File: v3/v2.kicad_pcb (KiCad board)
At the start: 2 copper layers, 82 parts, among them J1 Conn_01x05_Pin, SW1 SW_Push, SW10 SW_Push, SW11 SW_Push, SW12 SW_Push, SW13 SW_Push, SW14 SW_Push, SW15 SW_Push, SW16 SW_Push, SW17 SW_Push, SW18 SW_Push, SW19 SW_Push, SW2 SW_Push, SW20 SW_Push, SW21 SW_Push, SW22 SW_Push, SW23 SW_Push, SW24 SW_Push, SW25 SW_Push, SW26 SW_Push, SW27 SW_Push, SW28 SW_Push, SW29 SW_Push, SW3 SW_Push, SW30 SW_Push, SW31 SW_Push, SW32 SW_Push, SW33 RotaryEncoder_Switch, SW4 SW_Push, SW5 SW_Push, SW6 SW_Push, SW7 SW_Push, SW8 SW_Push, SW9 SW_Push, U1 nice_nano_left

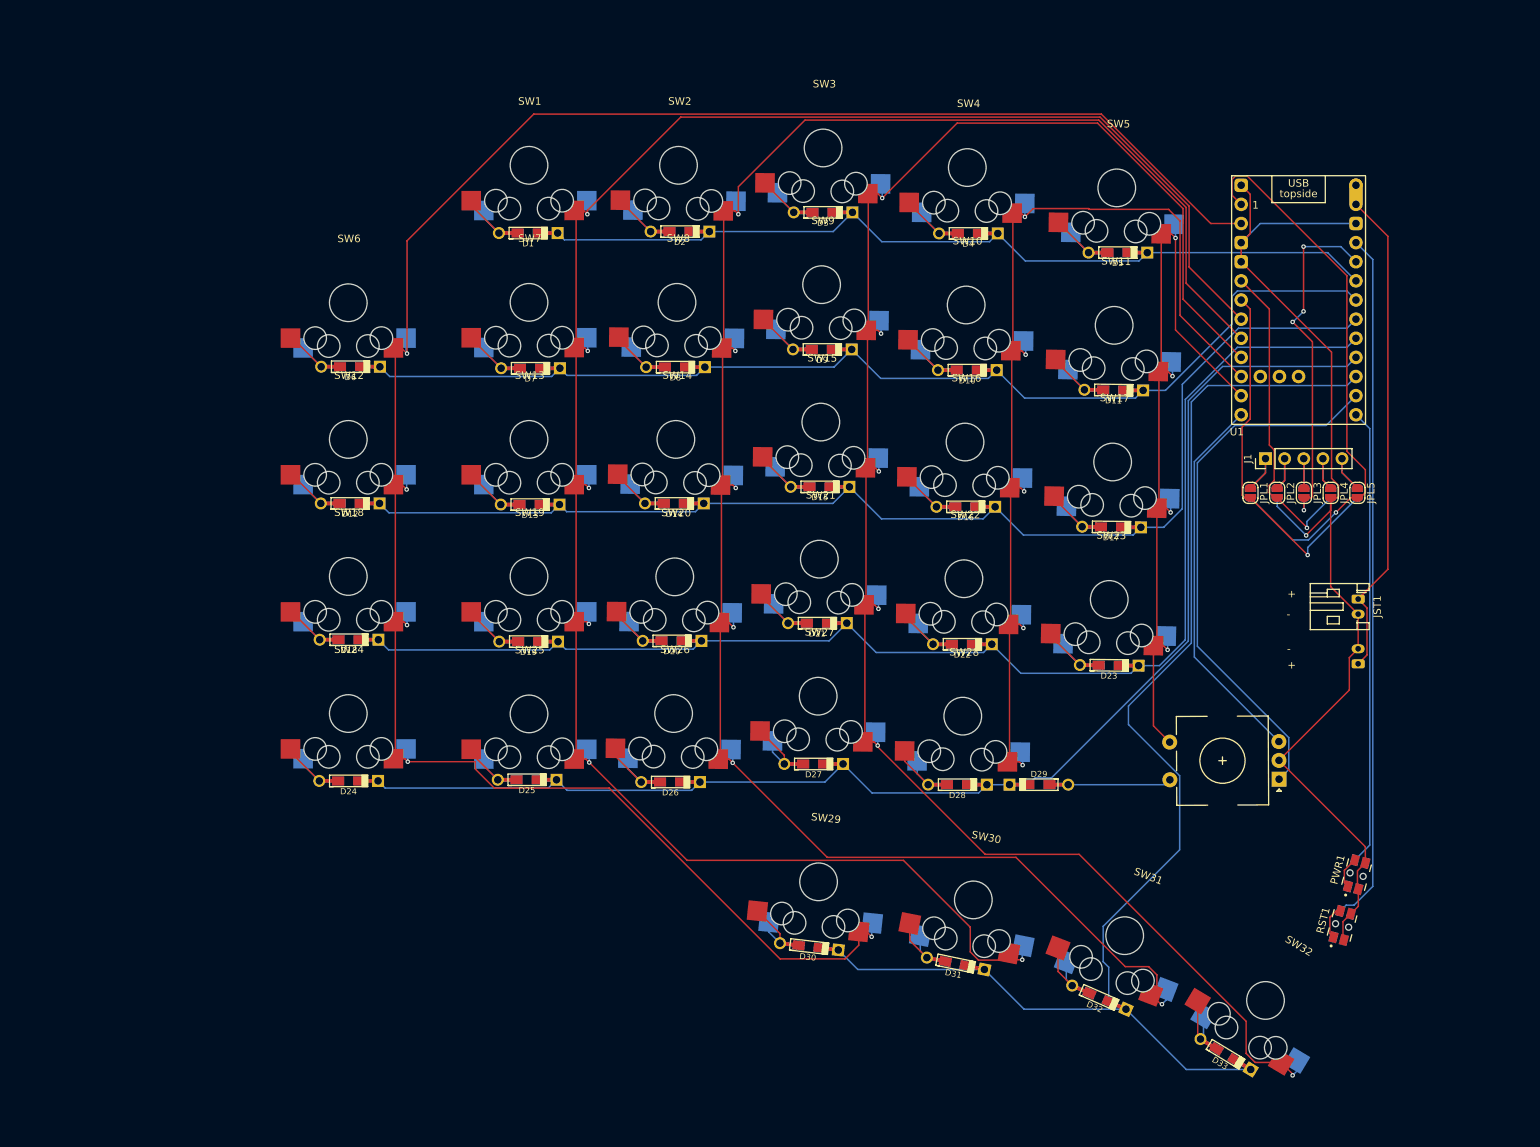
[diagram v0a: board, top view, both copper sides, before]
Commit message: added edge cuts and started cad again
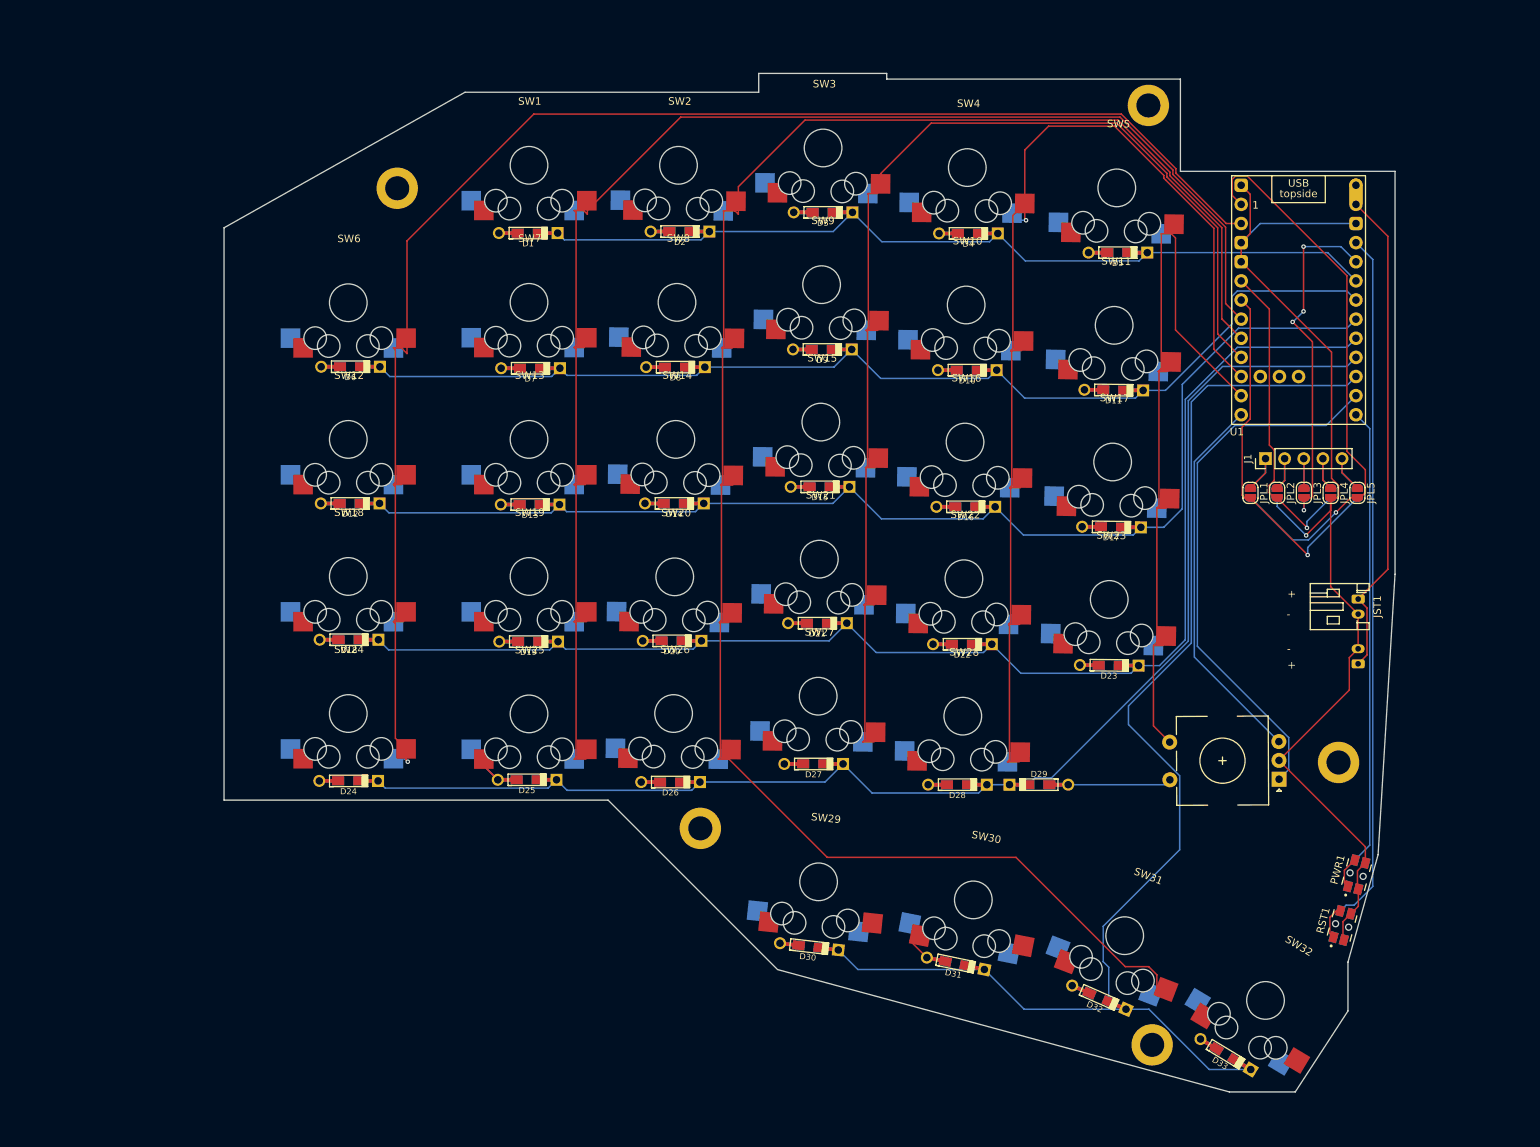
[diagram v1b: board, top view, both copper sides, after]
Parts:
- added REF**: MountingHole_3.2mm_M3_ISO14580_Pad, Keebio-Parts.pretty-master:MountingHole_3.2mm_M3_ISO14580_Pad, F.Cu at (250.8, 167.5)
- added REF**: MountingHole_3.2mm_M3_ISO14580_Pad, Keebio-Parts.pretty-master:MountingHole_3.2mm_M3_ISO14580_Pad, F.Cu at (250.2, 42.8)
- added REF**: MountingHole_3.2mm_M3_ISO14580_Pad, Keebio-Parts.pretty-master:MountingHole_3.2mm_M3_ISO14580_Pad, F.Cu at (275.5, 130.0)
- added REF**: MountingHole_3.2mm_M3_ISO14580_Pad, Keebio-Parts.pretty-master:MountingHole_3.2mm_M3_ISO14580_Pad, F.Cu at (150.5, 53.8)
- added REF**: MountingHole_3.2mm_M3_ISO14580_Pad, Keebio-Parts.pretty-master:MountingHole_3.2mm_M3_ISO14580_Pad, F.Cu at (190.8, 138.8)
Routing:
- net Col 4: track 243.3 -> 153.8 mm, vias 6 -> 0
- net Col 1: track 287.5 -> 201.9 mm, vias 5 -> 1
- net Col 2: track 274.4 -> 191.6 mm, vias 6 -> 0
- net Col 3: track 260.3 -> 245.2 mm, vias 6 -> 0
- net Col 6: track 109.6 -> 99.4 mm, vias 4 -> 0
- net Net-(D26-A): track 9.79 -> 0.00 mm
- net Net-(D24-A): track 9.67 -> 0.00 mm
- net Net-(D2-A): track 9.66 -> 0.00 mm
- net Net-(D1-A): track 9.65 -> 0.00 mm
- net Net-(D28-A): track 9.54 -> 0.00 mm
- net Net-(D23-A): track 9.53 -> 0.00 mm
- net Net-(D4-A): track 9.52 -> 0.00 mm
- net Net-(D27-A): track 9.43 -> 0.00 mm
- net Net-(D7-A): track 9.40 -> 0.00 mm
- net Net-(D10-A): track 9.35 -> 0.00 mm
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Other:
- board outline added: 155.5 x 135.2 mm

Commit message: fix lots of reversible error stuff
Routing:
- net Col 4: track 153.8 -> 255.2 mm, vias 0 -> 6
- net Col 2: track 191.6 -> 281.7 mm, vias 0 -> 6
- net Col 1: track 201.9 -> 284.0 mm, vias 1 -> 5
- net Col 3: track 245.2 -> 265.2 mm, vias 0 -> 6
- net Col 5: track 147.0 -> 165.1 mm, vias 1 -> 5
- net Col 6: track 99.4 -> 112.9 mm, vias 0 -> 4
- net Net-(D22-A): track 0.00 -> 9.01 mm, vias 0 -> 1
- net Net-(D23-A): track 0.00 -> 8.94 mm, vias 0 -> 1
- net Net-(D4-A): track 0.00 -> 8.91 mm, vias 0 -> 1
- net Net-(D9-A): track 0.00 -> 8.90 mm, vias 0 -> 1
- net Net-(D11-A): track 0.00 -> 8.84 mm, vias 0 -> 1
- net Net-(D26-A): track 0.00 -> 8.70 mm, vias 0 -> 1
- net Net-(D5-A): track 0.00 -> 8.69 mm, vias 0 -> 1
- net Net-(D17-A): track 0.00 -> 8.69 mm, vias 0 -> 1
- net Net-(D15-A): track 0.00 -> 8.67 mm, vias 0 -> 1
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
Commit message: added branding
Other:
- board text added: "Foxxboard V3"

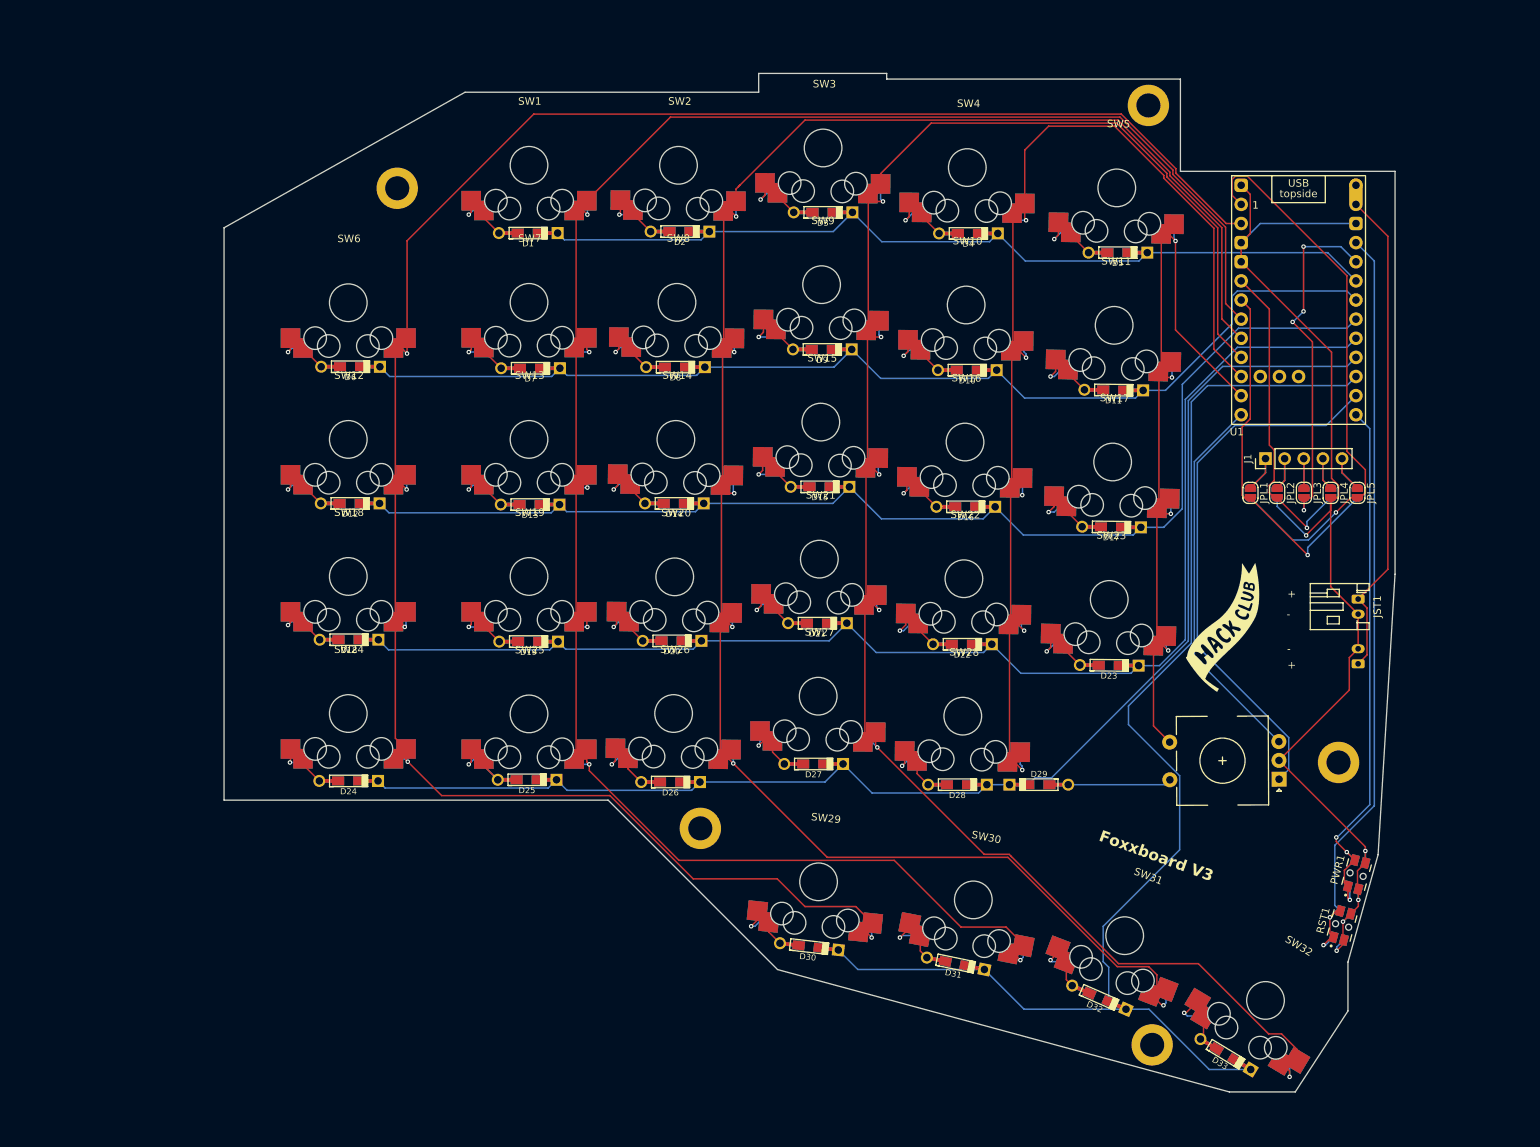
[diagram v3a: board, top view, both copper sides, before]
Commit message: added ground pads
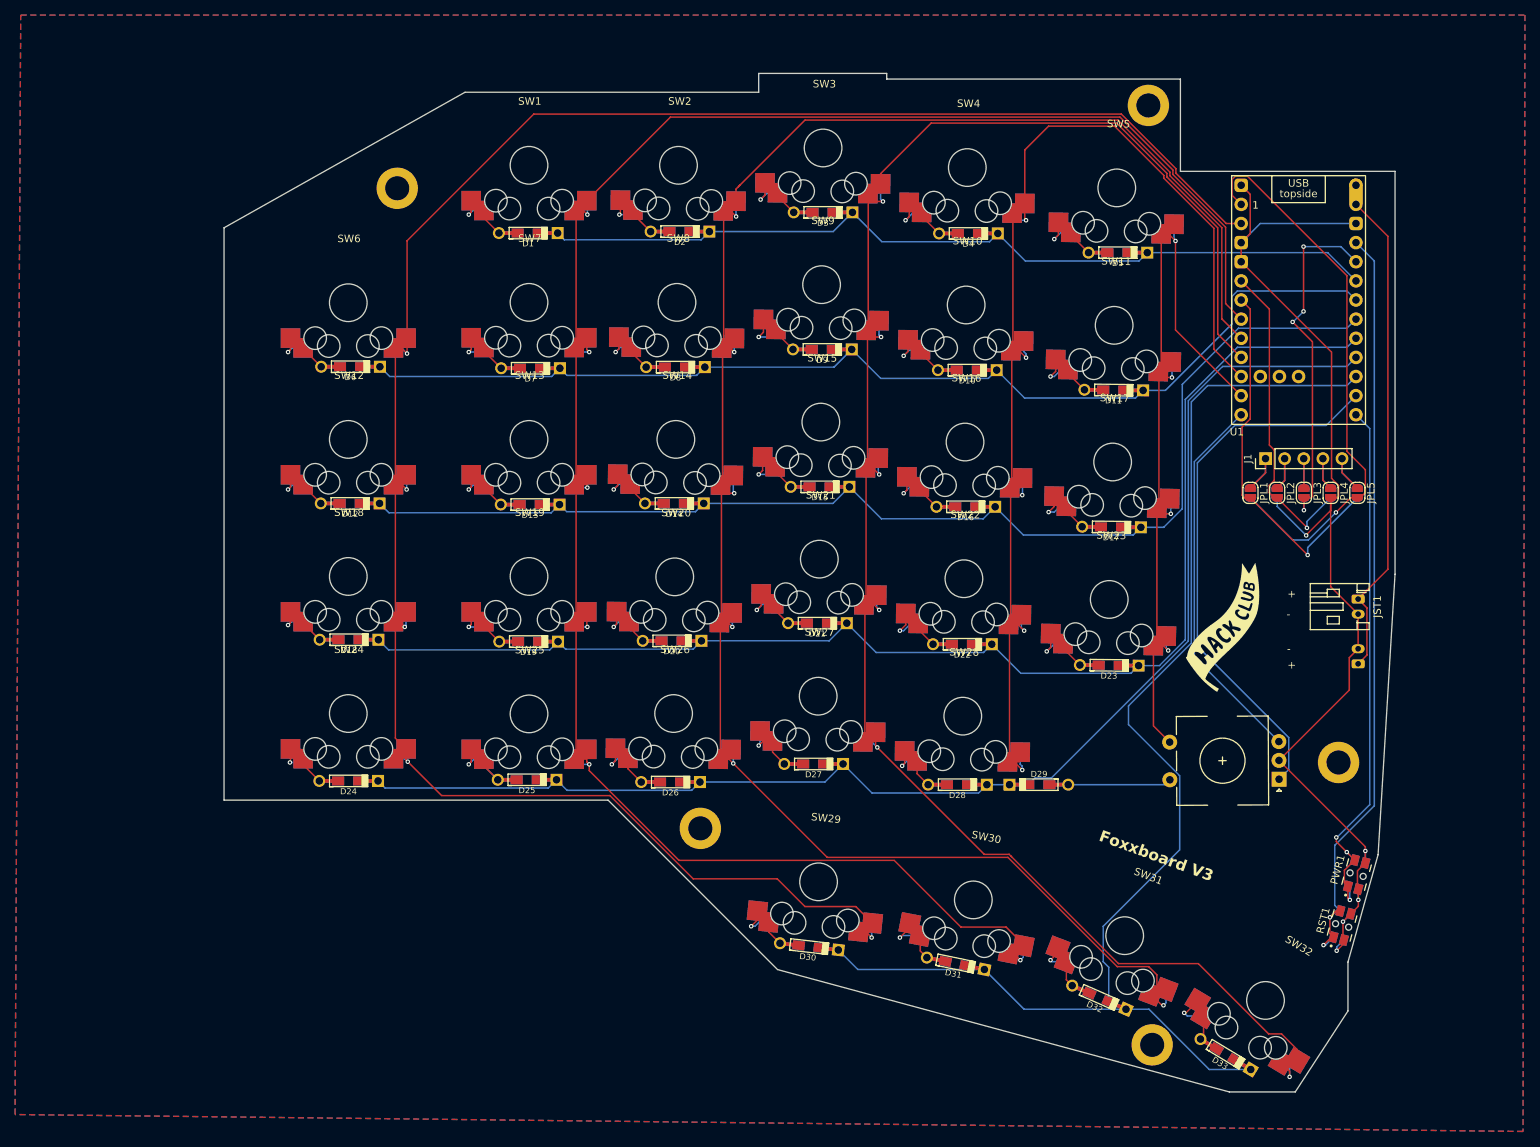
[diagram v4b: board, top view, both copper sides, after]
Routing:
- added copper zone on B.Cu, net GND
- added copper zone on F.Cu, net GND
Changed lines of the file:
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@@
 		(net 60)
+	)
+	(zone
+		(net 48)
+		(net_name "GND")
+		(layers "F&B.Cu")
+		(hatch edge 0.5)
+		(connect_pads
+			(clearance 0.5)
+		)
+		(min_thickness 0.25)
+		(filled_areas_thickness no)
+		(fill yes
+			(thermal_gap 0.5)
+			(thermal_bridge_width 0.5)
+			(island_removal_mode 2)
+			(island_area_min 10)
+		)
+		(polygon
+			(pts
+				(xy 300.25 30.75) (xy 300 179) (xy 99.75 176.75) (xy 100.5 30.75)
+			)
+		)
 	)
 	(group ""

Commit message: uhh nothing to pull so maybe an actual commit?
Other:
- board size 155.5 x 135.2 mm -> 158.5 x 135.2 mm
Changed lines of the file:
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@@
 		(pts
 			(xy 254.5 51.5) (xy 254.5 39.25) (xy 215.5 39.25) (xy 215.5 38.5) (xy 198.5 38.5) (xy 198.5 41) (xy 159.5 41)
-			(xy 127.5 59) (xy 127.5 135) (xy 178.5 135) (xy 201 157.5) (xy 261 173.75) (xy 269.75 173.75) (xy 276.75 163)
+			(xy 124.5 59) (xy 124.5 135) (xy 178.5 135) (xy 201 157.5) (xy 261 173.75) (xy 269.75 173.75) (xy 276.75 163)
 			(xy 276.75 156.5) (xy 280.75 142.25) (xy 283 105) (xy 283 51.5)
 		)
